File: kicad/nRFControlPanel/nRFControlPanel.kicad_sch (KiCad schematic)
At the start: 11 parts, among them J1 Power, J2 Digital/PWM, J3 Analog, J4 Digital/PWM, SW1 SW_Push, SW2 SW_Push, SW4 SW_Push, U1 RC1602A, U2 NRF24L01_Breakout

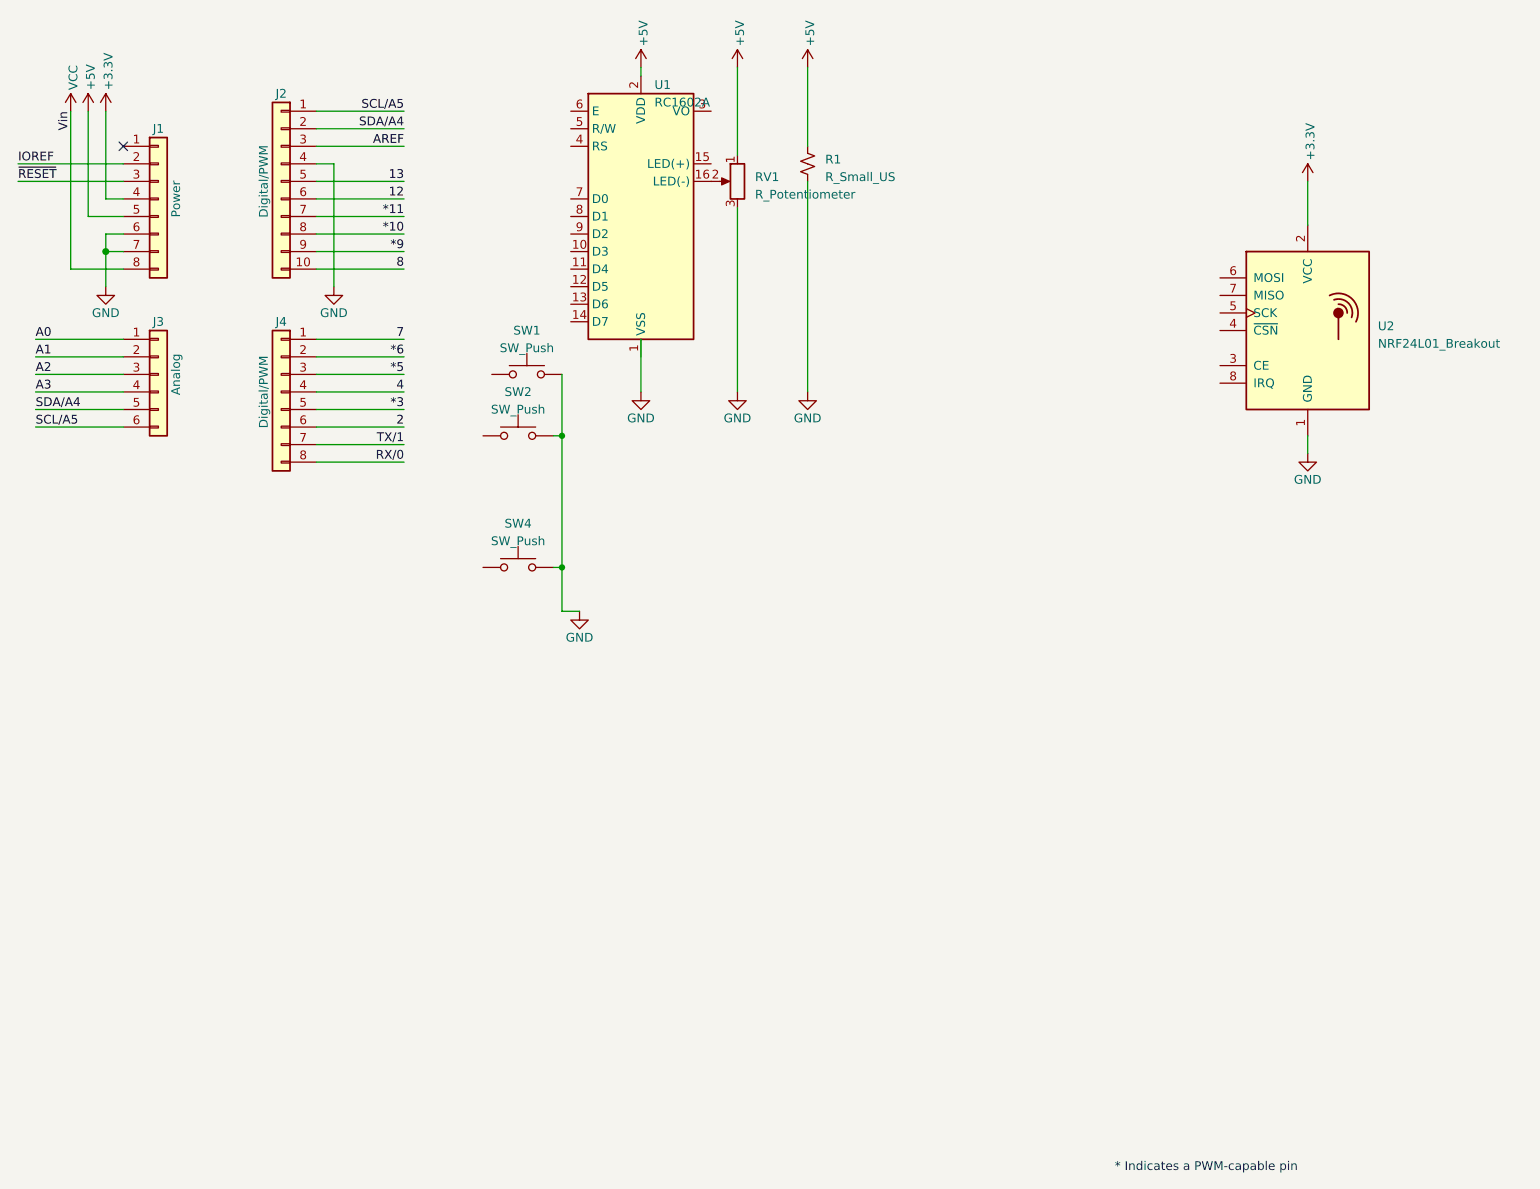
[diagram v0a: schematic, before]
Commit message: roughed out schematic for nRFControlPanel. Have not finished assigning pins to allow flexible layout.
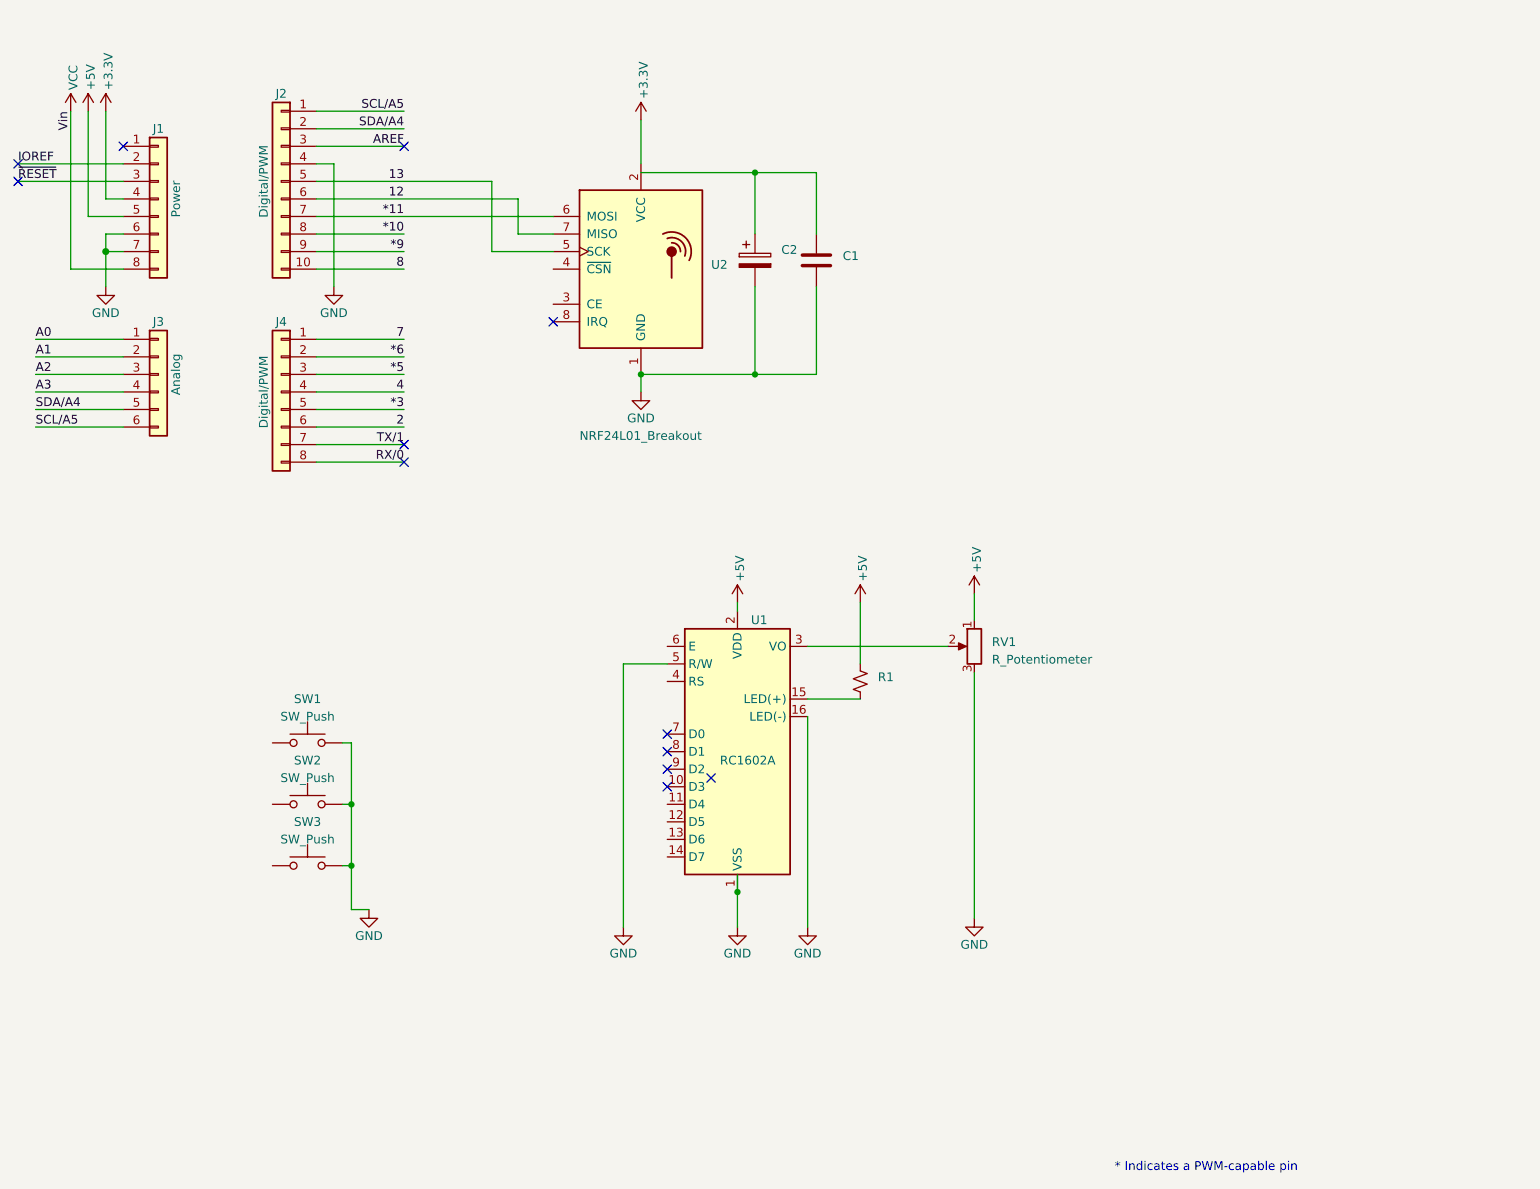
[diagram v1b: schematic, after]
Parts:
- added C1: C, symbol Device:C
- added C2: C_Polarized, symbol Device:C_Polarized
- renumbered SW4 to SW3
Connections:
- net *11: now also U2.6 (MOSI)
- net 12: now also U2.7 (MISO)
- net 13: now also U2.5 (SCK)
- net GND: now also U1.1 (VSS), U1.16 (LED(-)), U1.5 (R/W), C1.2, C2.2; no longer R1.2
- net at U1.15 (LED(+)): now also R1.2
- net at RV1.2: now also U1.3 (VO); no longer U1.16 (LED(-))
- new net: C1.1, C2.1
- no-connect marks 1 -> 12
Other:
- moved on the sheet: R1, RV1, SW1, SW2, SW3, U1, U2
